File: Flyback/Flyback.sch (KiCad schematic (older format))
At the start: 52 parts, among them Q1 IRF840, U1 UC3843_DIP8

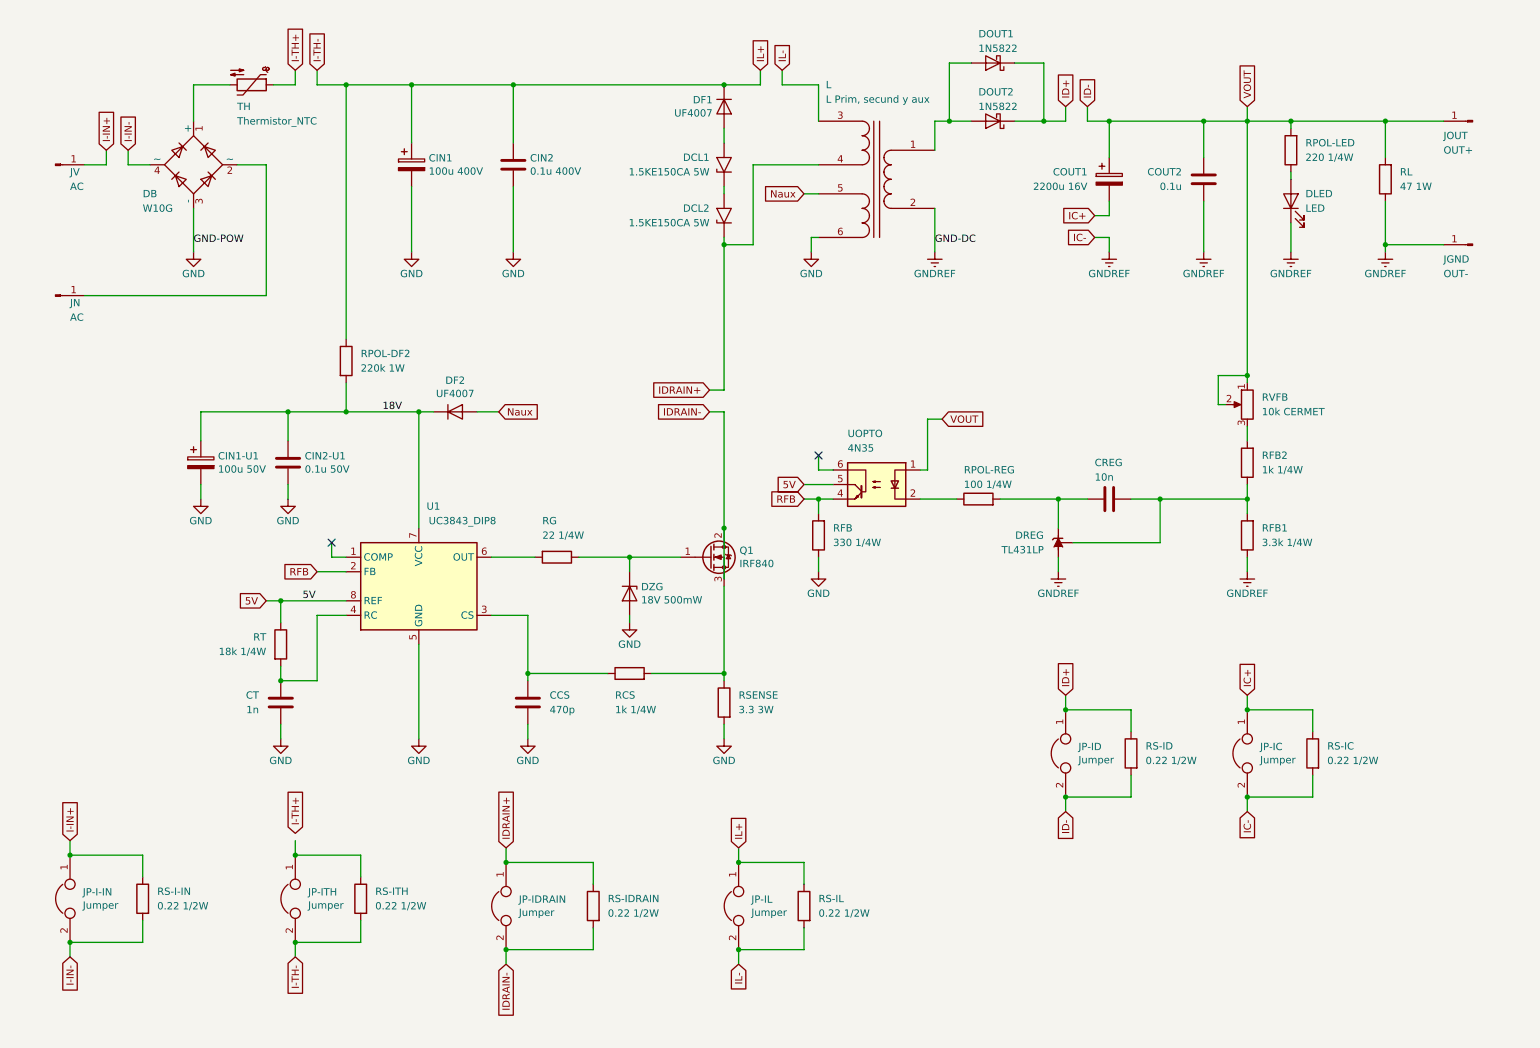
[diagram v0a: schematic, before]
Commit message: fixeado segun el esquematico que paso el prof
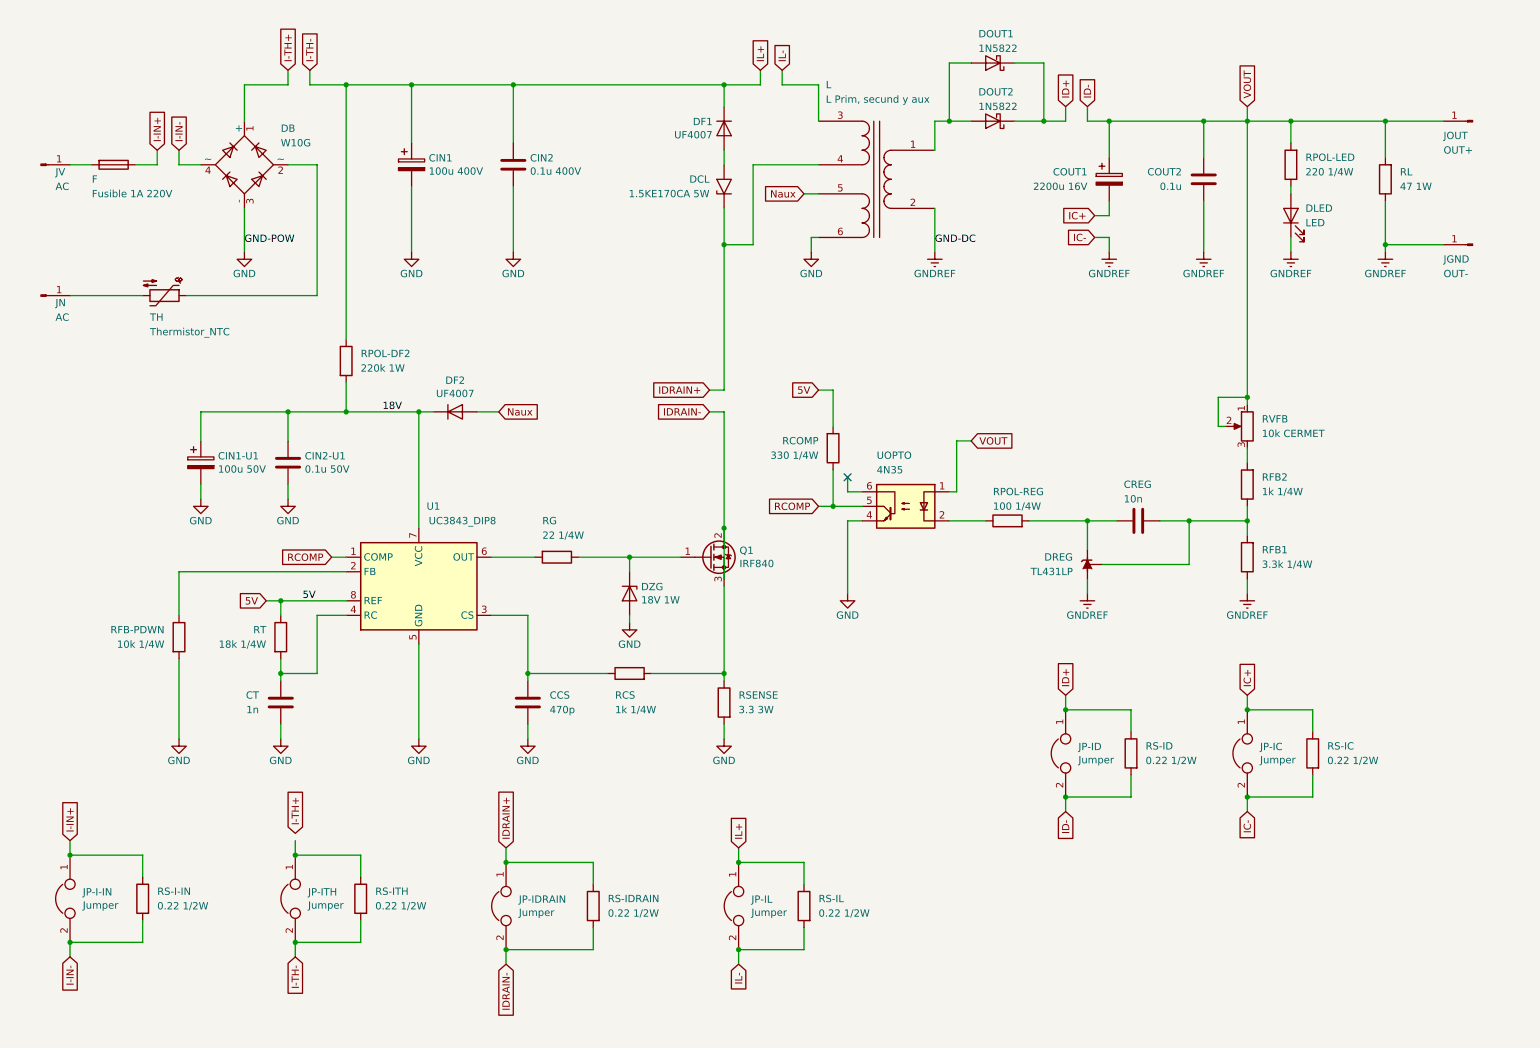
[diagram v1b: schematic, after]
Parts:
- removed DCL2: 1.5KE150CA 5W, Diode_THT:D_DO-201AE_P15.24mm_Horizontal, symbol Diode:1.5KExxA
- added F: Fusible 1A 220V, symbol Device:Fuse
- added RFB-PDWN: 10k 1/4W, symbol Device:R
- DCL: renamed from DCL1; value 1.5KE150CA 5W -> 1.5KE170CA 5W
- DZG: value 18V 500mW -> 18V 1W
- renumbered RFB to RCOMP
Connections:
- net 5V: now also RCOMP.2; no longer UOPTO.5
- net GND: now also UOPTO.4, RFB-PDWN.2; no longer RCOMP.1
- net I-IN+: now also F.1; no longer JV.1 (Pin_1)
- net I-TH+: now also DB.1 (+); no longer TH.1
- net IDRAIN+: now also DCL.1 (A1)
- net at TH.2: now also JN.1 (Pin_1); no longer DB.1 (+)
- net at DB.2 (~~): now also TH.1; no longer JN.1 (Pin_1)
- net RCOMP: now reaches U1.1 (COMP)
- net RCOMP: now also RCOMP.1, UOPTO.5
- removed net RFB: RCOMP.2, U1.2 (FB), UOPTO.4
- new net: F.2, JV.1 (Pin_1)
- new net: RFB-PDWN.1, U1.2 (FB)
- no-connect marks 2 -> 1
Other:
- moved on the sheet: CREG, DB, DCL, DF1, DLED, DREG, JN, JV, RCOMP, RFB1, RFB2, RPOL-LED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

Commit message: arreglos menores
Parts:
- added CMASAS: 1n 500V, symbol Device:C
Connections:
- net GND: now also CMASAS.1
- net GNDREF: now also CMASAS.2
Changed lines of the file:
@@
 Wire Wire Line
 	1800 4950 1800 5500
+$Comp
+L power:GND #PWR?
+U 1 1 5DB0EB5B
+P 6400 5500
+F 0 "#PWR?" H 6400 5250 50  0001 C CNN
+F 1 "GND" H 6400 5350 50  0000 C CNN
+F 2 "" H 6400 5500 50  0001 C CNN
+F 3 "" H 6400 5500 50  0001 C CNN
+	1    6400 5500
+	1    0    0    -1
+$EndComp
+$Comp
+L power:GNDREF #PWR?
+U 1 1 5DB17D5A
+P 7100 5500
+F 0 "#PWR?" H 7100 5250 50  0001 C CNN
+F 1 "GNDREF" H 7100 5350 50  0000 C CNN
+F 2 "" H 7100 5500 50  0001 C CNN
+F 3 "" H 7100 5500 50  0001 C CNN
+	1    7100 5500
+	1    0    0    -1
+$EndComp
+$Comp
+L Device:C CMASAS
+U 1 1 5DB345A9
+P 6750 5350
+F 0 "CMASAS" V 7000 5450 50  0000 R CNN
+F 1 "1n 500V" V 6900 5450 50  0000 R CNN
+F 2 "" H 6788 5200 50  0001 C CNN
+F 3 "~" H 6750 5350 50  0001 C CNN
+	1    6750 5350
+	0    -1   -1   0
+$EndComp
+Wire Wire Line
+	6600 5350 6400 5350
+Wire Wire Line
+	6400 5350 6400 5500
+Wire Wire Line
+	6900 5350 7100 5350
+Wire Wire Line
+	7100 5350 7100 5500
 $EndSCHEMATC

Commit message: primeros pasos del pcb
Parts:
- renumbered CCS to CCS1, CMASAS to CMASAS1, CREG to CREG1, CT to CT1, DB to DB1, DCL to DCL1, DLED to DLED1, DREG to DREG1, DZG to DZG1, F to F1, JGND to JGND1, JN to JN1, JOUT to JOUT1, JP-I-IN to JP-I-IN1, JP-IC to JP-IC1, JP-ID to JP-ID1, JP-IDRAIN to JP-IDRAIN1, JP-IL to JP-IL1, JP-ITH to JP-ITH1, JV to JV1, L to L1, RCOMP to RCOMP1, RCS to RCS1, RFB-PDWN to RFB-PDWN1, RG to RG1, RL to RL1, RPOL-LED to RPOL-LED1, RPOL-REG to RPOL-REG1, RS-I-IN to RS-I-IN1, RS-IC to RS-IC1, RS-ID to RS-ID1, RS-IDRAIN to RS-IDRAIN1, RS-IL to RS-IL1, RS-ITH to RS-ITH1, RSENSE to RSENSE1, RT to RT1, RVFB to RVFB1, TH to TH1, UOPTO to UOPTO1

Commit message: agregados packages de los componentes
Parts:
- removed F1: Fusible 1A 220V, symbol Device:Fuse
- removed RL1: 47 1W, symbol Device:R
- CCS1, CIN2-U1, COUT2, CREG1, CT1: footprint (none) -> Capacitor_THT:C_Disc_D3.8mm_W2.6mm_P2.50mm
- CIN1: footprint (none) -> Capacitor_THT:C_Radial_D18.0mm_H35.5mm_P7.50mm
- CIN1-U1: footprint (none) -> Capacitor_THT:C_Radial_D8.0mm_H11.5mm_P3.50mm
- CIN2: footprint (none) -> Capacitor_THT:C_Axial_L3.8mm_D2.6mm_P10.00mm_Horizontal
- CMASAS1: value 1n 500V -> 4.7n 2000V; footprint (none) -> Capacitor_THT:C_Disc_D6.0mm_W2.5mm_P5.00mm
- COUT1: footprint (none) -> Capacitor_THT:C_Radial_D12.5mm_H25.0mm_P5.00mm
- DLED1: footprint (none) -> LED_THT:LED_D5.0mm
- JGND1, JN1, JOUT1, JV1: footprint (none) -> Connector:Banana_Jack_1Pin
- JP-I-IN1, JP-IC1, JP-ID1, JP-IDRAIN1, JP-IL1, JP-ITH1: footprint (none) -> Connector_PinHeader_2.54mm:PinHeader_1x02_P2.54mm_Vertical
- RCOMP1, RCS1, RFB-PDWN1, RFB1, RFB2, RG1, RPOL-DF2, RPOL-LED1, RPOL-REG1, RT1: footprint (none) -> Resistor_THT:R_Axial_DIN0207_L6.3mm_D2.5mm_P10.16mm_Horizontal
- RVFB1: footprint (none) -> Potentiometer_THT:Potentiometer_Bourns_3266Y_Vertical
- TH1: footprint (none) -> Resistor_THT:R_Axial_DIN0207_L6.3mm_D2.5mm_P2.54mm_Vertical
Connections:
- net I-IN+: now also JV1.1 (Pin_1)

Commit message: Listo
Listo para el route
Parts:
- added F1: 250V 1A, Fuse:Fuseholder_Cylinder-5x20mm_Stelvio-Kontek_PTF78_Horizontal_Open, symbol Device:Fuse
- DREG1: footprint Package_TO_SOT_THT:TO-92_Inline -> Package_TO_SOT_THT:TO-92L_Wide
- L1: footprint (none) -> Flyback:Trafo-E30157; symbol Device:Transformer_1P_2S -> FlybackSymbol:Trafo-E30157
- RFB2: value 1k 1/4W -> 2.7k 1/4W
- RVFB1: value 10k CERMET -> 1k CERMET
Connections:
- net GND: now also L1.5; no longer L1.6 (SD)
- net GNDREF: now also L1.6; no longer L1.2 (AB)
- net I-IN+: now also F1.1; no longer JV1.1 (Pin_1)
- net I-TH+: now also JP-ITH1.1, RS-ITH1.1
- net IDRAIN+: now also L1.2; no longer L1.4 (SB)
- net IL-: now also L1.1; no longer L1.3 (SA)
- net Naux: now also L1.4; no longer L1.5 (SC)
- net at DOUT1.2 (A), DOUT2.2 (A): now also L1.10; no longer L1.1 (AA)
- new net: F1.2, JV1.1 (Pin_1)
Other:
- moved on the sheet: JP-I-IN1, RS-I-IN1
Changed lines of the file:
@@
 F 0 "DREG1" V 8100 4200 50  0000 R CNN
 F 1 "TL431LP" V 8000 4200 50  0000 R CNN
-F 2 "Package_TO_SOT_THT:TO-92_Inline" H 8050 4150 50  0001 C CIN
+F 2 "Package_TO_SOT_THT:TO-92L_Wide" H 8050 4150 50  0001 C CIN
 F 3 "http://www.ti.com/lit/ds/symlink/tl431.pdf" H 8050 4300 50  0001 C CIN
 	1    8050 4300
@@
 P 9150 3750
 F 0 "RFB2" H 9050 3700 50  0000 R CNN
-F 1 "1k 1/4W" H 9050 3800 50  0000 R CNN
+F 1 "2.7k 1/4W" H 9050 3800 50  0000 R CNN
 F 2 "Resistor_THT:R_Axial_DIN0207_L6.3mm_D2.5mm_P10.16mm_Horizontal" V 9080 3750 50  0001 C CNN
 F 3 "~" H 9150 3750 50  0001 C CNN
@@
 P 9150 3350
 F 0 "RVFB1" H 9050 3400 50  0000 R CNN
-F 1 "10k CERMET" H 9050 3300 50  0000 R CNN
+F 1 "1k CERMET" H 9050 3300 50  0000 R CNN
 F 2 "Potentiometer_THT:Potentiometer_Bourns_3266Y_Vertical" H 9150 3350 50  0001 C CNN
 F 3 "~" H 9150 3350 50  0001 C CNN
@@
 	5750 1550 6200 1550
 $Comp
-L Device:Transformer_1P_2S L1
+L FlybackSymbol:Trafo-E30157 L1
 U 1 1 5D902CE5
 P 6600 1650
 F 0 "L1" H 6950 2300 50  0000 R CNN
 F 1 "L Prim, secund y aux" H 6950 2200 50  0000 R CNN
-F 2 "" H 6600 1650 50  0001 C CNN
+F 2 "Flyback:Trafo-E30157" H 6600 1650 50  0001 C CNN
 F 3 "~" H 6600 1650 50  0001 C CNN
 	1    6600 1650
-	-1   0    0    -1
+	1    0    0    -1
 $EndComp
 Wire Wire Line
@@
 Text GLabel 4050 6250 1    50   Input ~ 0
 IDRAIN+
-Text GLabel 1050 7000 3    50   Input ~ 0
+Text GLabel 1300 7000 3    50   Input ~ 0
 I-IN-
-Text GLabel 1050 6200 1    50   Input ~ 0
+Text GLabel 1300 6200 1    50   Input ~ 0
 I-IN+
 NoConn ~ 6400 3700
@@
 Wire Wire Line
 	8200 2050 8200 2150
-Text GLabel 2600 6150 1    50   Input ~ 0
+Text GLabel 2600 6200 1    50   Input ~ 0
 I-TH+
 Text GLabel 2600 7000 3    50   Input ~ 0
@@
 L Device:R RS-I-IN1
 U 1 1 5DDB928A
-P 1550 6600
-F 0 "RS-I-IN1" H 1450 6650 50  0000 R CNN
-F 1 "0.22 1/2W" H 1450 6550 50  0000 R CNN
-F 2 "Resistor_THT:R_Axial_DIN0309_L9.0mm_D3.2mm_P15.24mm_Horizontal" V 1480 6600 50  0001 C CNN
-F 3 "~" H 1550 6600 50  0001 C CNN
-	1    1550 6600
+P 1800 6600
+F 0 "RS-I-IN1" H 1700 6650 50  0000 R CNN
+F 1 "0.22 1/2W" H 1700 6550 50  0000 R CNN
+F 2 "Resistor_THT:R_Axial_DIN0309_L9.0mm_D3.2mm_P15.24mm_Horizontal" V 1730 6600 50  0001 C CNN
+F 3 "~" H 1800 6600 50  0001 C CNN
+	1    1800 6600
 	-1   0    0    -1
 $EndComp
 Wire Wire Line
-	1050 6200 1050 6300
-Wire Wire Line
-	1550 6300 1550 6450
-Connection ~ 1050 6300
-Wire Wire Line
-	1550 6750 1550 6900
-Wire Wire Line
-	1050 6900 1050 7000
+	1300 6200 1300 6300
+Wire Wire Line
+	1800 6300 1800 6450
+Connection ~ 1300 6300
+Wire Wire Line
+	1800 6750 1800 6900
+Wire Wire Line
+	1300 6900 1300 7000
 $Comp
 L Device:Jumper JP-I-IN1
 U 1 1 5DDB9298
-P 1050 6600
-F 0 "JP-I-IN1" V 1004 6512 50  0000 R CNN
-F 1 "Jumper" V 1095 6512 50  0000 R CNN
-F 2 "Connector_PinHeader_2.54mm:PinHeader_1x02_P2.54mm_Vertical" H 1050 6600 50  0001 C CNN
-F 3 "~" H 1050 6600 50  0001 C CNN
-	1    1050 6600
+P 1300 6600
+F 0 "JP-I-IN1" V 1254 6512 50  0000 R CNN
+F 1 "Jumper" V 1345 6512 50  0000 R CNN
+F 2 "Connector_PinHeader_2.54mm:PinHeader_1x02_P2.54mm_Vertical" H 1300 6600 50  0001 C CNN
+F 3 "~" H 1300 6600 50  0001 C CNN
+	1    1300 6600
 	0    -1   1    0
 $EndComp
 Wire Wire Line
-	1050 6300 1550 6300
-Wire Wire Line
-	1050 6900 1550 6900
-Connection ~ 1050 6900
+	1300 6300 1800 6300
+Wire Wire Line
+	1300 6900 1800 6900
+Connection ~ 1300 6900
 Wire Wire Line
 	4050 6350 4650 6350
@@
 Wire Wire Line
 	9450 1250 10500 1250
-Wire Wire Line
-	1050 1550 1650 1550
+$Comp
+L Device:Fuse F1
+U 1 1 5D9966CE
+P 1350 1550
+F 0 "F1" V 1153 1550 50  0000 C CNN
+F 1 "250V 1A" V 1244 1550 50  0000 C CNN
+F 2 "Fuse:Fuseholder_Cylinder-5x20mm_Stelvio-Kontek_PTF78_Horizontal_Open" V 1280 1550 50  0001 C CNN
+F 3 "~" H 1350 1550 50  0001 C CNN
+	1    1350 1550
+	0    1    1    0
+$EndComp
+Wire Wire Line
+	1500 1550 1650 1550
+Wire Wire Line
+	1050 1550 1200 1550
 $EndSCHEMATC
